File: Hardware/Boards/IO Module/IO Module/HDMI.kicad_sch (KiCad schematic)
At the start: 57 parts, among them J4 HDMI_A, U19 TPS74801AWDRC, U20 SN75DP159RGZ, U21 TXB0108DQSR, U22 TXB0101DCK

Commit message: Completed IO Module PCB Layout
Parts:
- R80: value 10K -> 100K
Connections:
- net +3V3: now also R80.2
- net GND: no longer R80.1
- net HDMI_F_I2C_EN: now also U21.1 (A1); no longer U21.2 (A2)
- net HDMI_F_SWAP: now also U21.2 (A2); no longer U21.1 (A1)
- net HDMI_I2C_EN: now also U21.20 (B1); no longer U21.19 (B2)
- net HDMI_SWAP: now also U21.19 (B2); no longer U21.20 (B1)
- net at U21.6 (OE): now also R80.1; no longer R80.2
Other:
- moved on the sheet: R80
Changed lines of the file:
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@@
 	(wire
 		(pts
-			(xy 275.59 123.19) (xy 273.05 123.19)
-		)
-		(stroke
-			(width 0)
-			(type default)
-		)
-	)
-	(wire
-		(pts
 			(xy 340.36 101.6) (xy 340.36 102.87)
 		)
@@
 	(wire
 		(pts
-			(xy 273.05 156.21) (xy 273.05 157.48)
-		)
-		(stroke
-			(width 0)
-			(type default)
-		)
-	)
-	(wire
-		(pts
 			(xy 106.68 213.36) (xy 106.68 194.31)
 		)
@@
 	(wire
 		(pts
+			(xy 266.7 123.19) (xy 266.7 121.92)
+		)
+		(stroke
+			(width 0)
+			(type default)
+		)
+	)
+	(wire
+		(pts
 			(xy 31.75 54.61) (xy 31.75 55.88)
 		)
@@
 	(wire
 		(pts
-			(xy 273.05 123.19) (xy 273.05 148.59)
-		)
-		(stroke
-			(width 0)
-			(type default)
-		)
-	)
-	(wire
-		(pts
 			(xy 97.79 196.85) (xy 100.33 196.85)
 		)
@@
 	(wire
 		(pts
+			(xy 266.7 123.19) (xy 275.59 123.19)
+		)
+		(stroke
+			(width 0)
+			(type default)
+		)
+	)
+	(wire
+		(pts
 			(xy 321.31 110.49) (xy 321.31 111.76)
 		)
@@
 	(wire
 		(pts
+			(xy 266.7 113.03) (xy 266.7 114.3)
+		)
+		(stroke
+			(width 0)
+			(type default)
+		)
+	)
+	(wire
+		(pts
 			(xy 167.64 120.65) (xy 191.77 120.65)
 		)
@@
 		)
 	)
-	(label "HDMI_F_SWAP"
-		(at 232.41 125.73 0)
-		(fields_autoplaced yes)
-		(effects
-			(font
-				(size 1.27 1.27)
-			)
-			(justify left bottom)
-		)
-	)
 	(label "HDMI_TX_TERM_CTL"
 		(at 321.31 138.43 180)
@@
 		)
 	)
+	(label "HDMI_F_SWAP"
+		(at 232.41 128.27 0)
+		(fields_autoplaced yes)
+		(effects
+			(font
+				(size 1.27 1.27)
+			)
+			(justify left bottom)
+		)
+	)
 	(label "HDMI_AUX_N"
 		(at 138.43 156.21 0)
@@
 		)
 	)
+	(label "HDMI_F_I2C_EN"
+		(at 232.41 125.73 0)
+		(fields_autoplaced yes)
+		(effects
+			(font
+				(size 1.27 1.27)
+			)
+			(justify left bottom)
+		)
+	)
 	(label "HDMI_D0_N"
 		(at 138.43 128.27 0)
@@
 		)
 	)
+	(label "HDMI_SWAP"
+		(at 321.31 128.27 180)
+		(fields_autoplaced yes)
+		(effects
+			(font
+				(size 1.27 1.27)
+			)
+			(justify right bottom)
+		)
+	)
 	(label "PP1V1H_FB"
 		(at 55.88 43.18 0)
@@
 		)
 	)
-	(label "HDMI_F_I2C_EN"
-		(at 232.41 128.27 0)
-		(fields_autoplaced yes)
-		(effects
-			(font
-				(size 1.27 1.27)
-			)
-			(justify left bottom)
-		)
-	)
-	(label "HDMI_SWAP"
-		(at 321.31 125.73 180)
-		(fields_autoplaced yes)
-		(effects
-			(font
-				(size 1.27 1.27)
-			)
-			(justify right bottom)
-		)
-	)
 	(label "HDMI_CON_CLK_P"
 		(at 259.08 68.58 0)
@@
 		)
 	)
+	(label "HDMI_I2C_EN"
+		(at 321.31 125.73 180)
+		(fields_autoplaced yes)
+		(effects
+			(font
+				(size 1.27 1.27)
+			)
+			(justify right bottom)
+		)
+	)
 	(label "HDMI_CEC"
 		(at 138.43 245.11 0)
@@
 		)
 	)
-	(label "HDMI_I2C_EN"
-		(at 321.31 128.27 180)
-		(fields_autoplaced yes)
-		(effects
-			(font
-				(size 1.27 1.27)
-			)
-			(justify right bottom)
-		)
-	)
 	(label "HDMI_F_EQ_SEL"
 		(at 232.41 133.35 0)
@@
 		)
 	)
-	(hierarchical_label "HDMI_SWAP"
-		(shape input)
-		(at 321.31 125.73 0)
-		(fields_autoplaced yes)
-		(effects
-			(font
-				(size 1.27 1.27)
-			)
-			(justify left)
-		)
-	)
 	(hierarchical_label "HDMI_CLK_P"
 		(shape input)
@@
 		)
 	)
-	(hierarchical_label "HDMI_I2C_EN"
-		(shape input)
-		(at 321.31 128.27 0)
-		(fields_autoplaced yes)
-		(effects
-			(font
-				(size 1.27 1.27)
-			)
-			(justify left)
-		)
-	)
 	(hierarchical_label "HDMI_D2_N"
 		(shape input)
@@
 		)
 	)
+	(hierarchical_label "HDMI_SWAP"
+		(shape input)
+		(at 321.31 128.27 0)
+		(fields_autoplaced yes)
+		(effects
+			(font
+				(size 1.27 1.27)
+			)
+			(justify left)
+		)
+	)
 	(hierarchical_label "FPGA_I2C_SDA"
 		(shape input)
@@
 		)
 	)
+	(hierarchical_label "HDMI_I2C_EN"
+		(shape input)
+		(at 321.31 125.73 0)
+		(fields_autoplaced yes)
+		(effects
+			(font
+				(size 1.27 1.27)
+			)
+			(justify left)
+		)
+	)
 	(hierarchical_label "FPGA_I2C_SCL"
 		(shape input)
@@
 	)
 	(symbol
-		(lib_id "power:GND")
-		(at 273.05 157.48 0)
-		(unit 1)
-		(exclude_from_sim no)
-		(in_bom yes)
-		(on_board yes)
-		(dnp no)
-		(property "Reference" "#PWR0245"
-			(at 273.05 161.29 0)
-			(effects
-				(font
-					(size 1.27 1.27)
-				)
-				(hide yes)
-			)
-		)
-		(property "Value" "GND"
-			(at 273.05 161.29 0)
-			(effects
-				(font
-					(size 1.27 1.27)
-				)
-			)
-		)
-		(property "Footprint" ""
-			(at 273.05 157.48 0)
-			(effects
-				(font
-					(size 1.27 1.27)
-				)
-				(hide yes)
-			)
-		)
-		(property "Datasheet" ""
-			(at 273.05 157.48 0)
-			(effects
-				(font
-					(size 1.27 1.27)
-				)
-				(hide yes)
-			)
-		)
-		(property "Description" "Power symbol creates a global label with name \"GND\" , ground"
-			(at 273.05 157.48 0)
-			(effects
-				(font
-					(size 1.27 1.27)
-				)
-				(hide yes)
-			)
-		)
-		(pin "1"
-		)
-		(instances
-			(project "IO Module"
-				(path "/884396b6-238b-495e-b731-e47ad2523f76/dcc99803-8acd-4632-9c0b-7f677477cf65/84e0983c-4a92-4326-b25d-d105fd964129"
-					(reference "#PWR0245")
-					(unit 1)
-				)
-			)
-		)
-	)
-	(symbol
 		(lib_id "power:+1V8")
 		(at 204.47 222.25 0)
@@
 	(symbol
 		(lib_id "Device:R_US")
-		(at 273.05 152.4 180)
+		(at 266.7 118.11 180)
 		(unit 1)
 		(exclude_from_sim no)
@@
 		(dnp no)
 		(property "Reference" "R80"
-			(at 277.495 153.67 0)
+			(at 271.145 119.38 0)
 			(effects
 				(font
@@
 			)
 		)
-		(property "Value" "10K"
-			(at 277.495 151.13 0)
+		(property "Value" "100K"
+			(at 271.145 116.84 0)
 			(effects
 				(font
@@
 		)
 		(property "Footprint" "Resistor_SMD:R_0201_0603Metric"
-			(at 272.034 152.146 90)
+			(at 265.684 117.856 90)
 			(effects
 				(font
@@
 		)
 		(property "Datasheet" "~"
-			(at 273.05 152.4 0)
+			(at 266.7 118.11 0)
 			(effects
 				(font
@@
 		)
 		(property "Description" "Resistor, US symbol"
-			(at 273.05 152.4 0)
+			(at 266.7 118.11 0)
 			(effects
 				(font
@@
 					(unit 1)
 				)
+			)
+		)
+	)
+	(symbol
+		(lib_id "power:+3V3")
+		(at 266.7 113.03 0)
+		(unit 1)
+		(exclude_from_sim no)
+		(in_bom yes)
+		(on_board yes)
+		(dnp no)
+		(property "Reference" "#PWR0159"
+			(at 266.7 116.84 0)
+			(effects
+				(font
+					(size 1.27 1.27)
+				)
+				(hide yes)
+			)
+		)
+		(property "Value" "+3V3"
+			(at 266.7 109.22 0)
+			(effects
+				(font
+					(size 1.27 1.27)
+				)
+			)
+		)
+		(property "Footprint" ""
+			(at 266.7 113.03 0)
+			(effects
+				(font
+					(size 1.27 1.27)
+				)
+				(hide yes)
+			)
+		)
+		(property "Datasheet" ""
+			(at 266.7 113.03 0)
+			(effects
+				(font
+					(size 1.27 1.27)
+				)
+				(hide yes)
+			)
+		)
+		(property "Description" "Power symbol creates a global label with name \"+3V3\""
+			(at 266.7 113.03 0)
+			(effects
+				(font
+					(size 1.27 1.27)
+				)
+				(hide yes)
+			)
+		)
+		(pin "1"
+		)
+		(instances
+			(project "IO Module"
+				(path "/884396b6-238b-495e-b731-e47ad2523f76/dcc99803-8acd-4632-9c0b-7f677477cf65/84e0983c-4a92-4326-b25d-d105fd964129"
+					(reference "#PWR0159")
+					(unit 1)
+				)

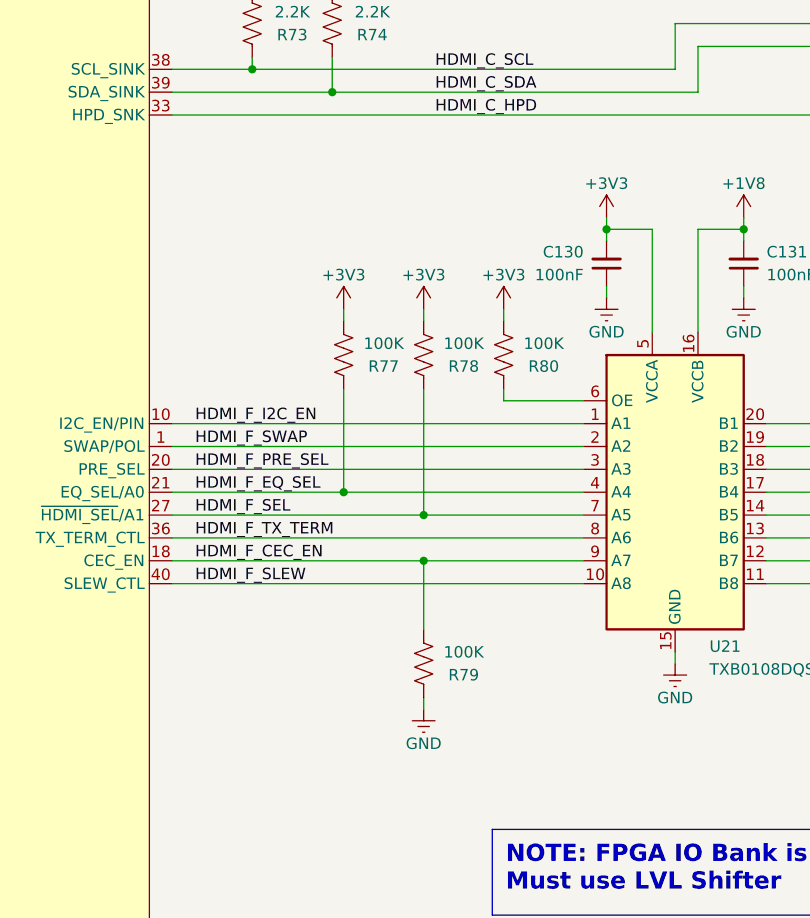
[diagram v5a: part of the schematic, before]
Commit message: Cleaned up routing for IO module
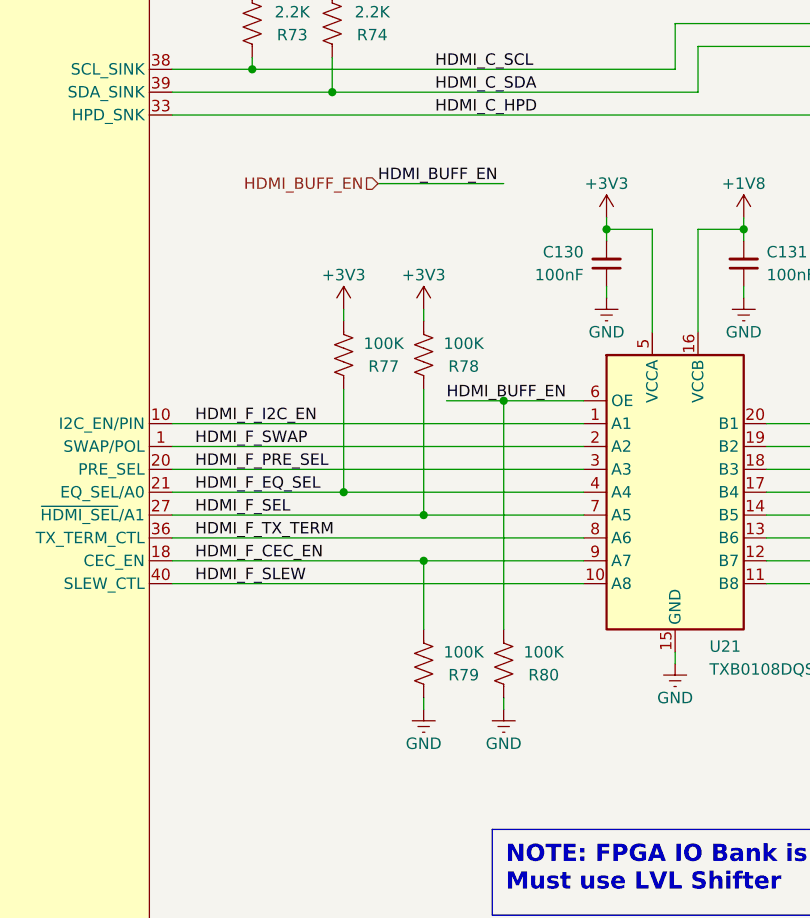
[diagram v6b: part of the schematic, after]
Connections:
- net +3V3: no longer R80.2
- net GND: now also R80.1
- net HDMI_BUFF_EN: now reaches U21.6 (OE)
- net HDMI_BUFF_EN: now also R80.2; no longer R80.1
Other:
- moved on the sheet: R80
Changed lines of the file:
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@@
 	)
 	(junction
+		(at 266.7 123.19)
+		(diameter 0)
+		(color 0 0 0 0)
+	)
+	(junction
 		(at 168.91 78.74)
 		(diameter 0)
@@
 	(wire
 		(pts
+			(xy 266.7 123.19) (xy 266.7 148.59)
+		)
+		(stroke
+			(width 0)
+			(type default)
+		)
+	)
+	(wire
+		(pts
 			(xy 154.94 184.15) (xy 191.77 184.15)
 		)
@@
 	(wire
 		(pts
-			(xy 266.7 123.19) (xy 266.7 121.92)
+			(xy 266.7 123.19) (xy 275.59 123.19)
 		)
 		(stroke
@@
 	(wire
 		(pts
+			(xy 266.7 156.21) (xy 266.7 157.48)
+		)
+		(stroke
+			(width 0)
+			(type default)
+		)
+	)
+	(wire
+		(pts
 			(xy 167.64 142.24) (xy 191.77 142.24)
 		)
@@
 	(wire
 		(pts
+			(xy 252.73 99.06) (xy 266.7 99.06)
+		)
+		(stroke
+			(width 0)
+			(type default)
+		)
+	)
+	(wire
+		(pts
 			(xy 190.5 55.88) (xy 191.77 55.88)
 		)
@@
 	(wire
 		(pts
-			(xy 266.7 123.19) (xy 275.59 123.19)
+			(xy 260.35 123.19) (xy 266.7 123.19)
 		)
 		(stroke
@@
 	(wire
 		(pts
-			(xy 266.7 113.03) (xy 266.7 114.3)
-		)
-		(stroke
-			(width 0)
-			(type default)
-		)
-	)
-	(wire
-		(pts
 			(xy 167.64 120.65) (xy 191.77 120.65)
 		)
@@
 		)
 	)
+	(label "HDMI_BUFF_EN"
+		(at 260.35 123.19 0)
+		(fields_autoplaced yes)
+		(effects
+			(font
+				(size 1.27 1.27)
+			)
+			(justify left bottom)
+		)
+	)
 	(label "HDMI_TX_TERM_CTL"
 		(at 321.31 138.43 180)
@@
 		)
 	)
+	(label "HDMI_BUFF_EN"
+		(at 252.73 99.06 0)
+		(fields_autoplaced yes)
+		(effects
+			(font
+				(size 1.27 1.27)
+			)
+			(justify left bottom)
+		)
+	)
 	(label "HDMI_CLK_N"
 		(at 138.43 142.24 0)
@@
 		)
 	)
+	(hierarchical_label "HDMI_BUFF_EN"
+		(shape input)
+		(at 252.73 99.06 180)
+		(fields_autoplaced yes)
+		(effects
+			(font
+				(size 1.27 1.27)
+			)
+			(justify right)
+		)
+	)
 	(hierarchical_label "HDMI_D2_N"
 		(shape input)
@@
 	(symbol
 		(lib_id "power:GND")
+		(at 266.7 157.48 0)
+		(unit 1)
+		(exclude_from_sim no)
+		(in_bom yes)
+		(on_board yes)
+		(dnp no)
+		(property "Reference" "#PWR088"
+			(at 266.7 161.29 0)
+			(effects
+				(font
+					(size 1.27 1.27)
+				)
+				(hide yes)
+			)
+		)
+		(property "Value" "GND"
+			(at 266.7 161.29 0)
+			(effects
+				(font
+					(size 1.27 1.27)
+				)
+			)
+		)
+		(property "Footprint" ""
+			(at 266.7 157.48 0)
+			(effects
+				(font
+					(size 1.27 1.27)
+				)
+				(hide yes)
+			)
+		)
+		(property "Datasheet" ""
+			(at 266.7 157.48 0)
+			(effects
+				(font
+					(size 1.27 1.27)
+				)
+				(hide yes)
+			)
+		)
+		(property "Description" "Power symbol creates a global label with name \"GND\" , ground"
+			(at 266.7 157.48 0)
+			(effects
+				(font
+					(size 1.27 1.27)
+				)
+				(hide yes)
+			)
+		)
+		(pin "1"
+		)
+		(instances
+			(project "IO Module"
+				(path "/884396b6-238b-495e-b731-e47ad2523f76/dcc99803-8acd-4632-9c0b-7f677477cf65/84e0983c-4a92-4326-b25d-d105fd964129"
+					(reference "#PWR088")
+					(unit 1)
+				)
+			)
+		)
+	)
+	(symbol
+		(lib_id "power:GND")
 		(at 167.64 60.96 0)
 		(unit 1)
@@
 	(symbol
 		(lib_id "Device:R_US")
-		(at 266.7 118.11 180)
+		(at 266.7 152.4 180)
 		(unit 1)
 		(exclude_from_sim no)
@@
 		(dnp no)
 		(property "Reference" "R80"
-			(at 271.145 119.38 0)
+			(at 271.145 153.67 0)
 			(effects
 				(font
@@
 		)
 		(property "Value" "100K"
-			(at 271.145 116.84 0)
+			(at 271.145 151.13 0)
 			(effects
 				(font
@@
 		)
 		(property "Footprint" "Resistor_SMD:R_0201_0603Metric"
-			(at 265.684 117.856 90)
+			(at 265.684 152.146 90)
 			(effects
 				(font
@@
 		)
 		(property "Datasheet" "~"
-			(at 266.7 118.11 0)
+			(at 266.7 152.4 0)
 			(effects
 				(font
@@
 		)
 		(property "Description" "Resistor, US symbol"
-			(at 266.7 118.11 0)
+			(at 266.7 152.4 0)
 			(effects
 				(font
@@
 					(unit 1)
 				)
-			)
-		)
-	)
-	(symbol
-		(lib_id "power:+3V3")
-		(at 266.7 113.03 0)
-		(unit 1)
-		(exclude_from_sim no)
-		(in_bom yes)
-		(on_board yes)
-		(dnp no)
-		(property "Reference" "#PWR0159"
-			(at 266.7 116.84 0)
-			(effects
-				(font
-					(size 1.27 1.27)
-				)
-				(hide yes)
-			)
-		)
-		(property "Value" "+3V3"
-			(at 266.7 109.22 0)
-			(effects
-				(font
-					(size 1.27 1.27)
-				)
-			)
-		)
-		(property "Footprint" ""
-			(at 266.7 113.03 0)
-			(effects
-				(font
-					(size 1.27 1.27)
-				)
-				(hide yes)
-			)
-		)
-		(property "Datasheet" ""
-			(at 266.7 113.03 0)
-			(effects
-				(font
-					(size 1.27 1.27)
-				)
-				(hide yes)
-			)
-		)
-		(property "Description" "Power symbol creates a global label with name \"+3V3\""
-			(at 266.7 113.03 0)
-			(effects
-				(font
-					(size 1.27 1.27)
-				)
-				(hide yes)
-			)
-		)
-		(pin "1"
-		)
-		(instances
-			(project "IO Module"
-				(path "/884396b6-238b-495e-b731-e47ad2523f76/dcc99803-8acd-4632-9c0b-7f677477cf65/84e0983c-4a92-4326-b25d-d105fd964129"
-					(reference "#PWR0159")
-					(unit 1)
-				)

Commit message: Using new DP to HDMI IC
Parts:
- removed C139, C141, C142: 100nF, Capacitor_SMD:C_0201_0603Metric, symbol Device:C_Small
- removed D8: BAS516, Diode_SMD:D_SOD-523, symbol Diode:BAS516
- removed R82: 1K, Resistor_SMD:R_0201_0603Metric, symbol Device:R_US
- removed R88: 27K, Resistor_SMD:R_0201_0603Metric, symbol Device:R_US
- removed U20: SN75DP159RGZ, Package_DFN_QFN:QFN-48-1EP_7x7mm_P0.5mm_EP5.1x5.1mm, symbol IO_Module:SN75DP159
- removed U22: TXB0101DCK, Package_TO_SOT_SMD:SOT-363_SC-70-6, symbol Logic_LevelTranslator:TXB0101DCK
- added C153: 1uF, Capacitor_SMD:C_0201_0603Metric, symbol Device:C_Small
- added C154, C155, C156, C43: 100nF, Capacitor_SMD:C_0201_0603Metric, symbol Device:C_Small
- added R34: 33R, Resistor_SMD:R_0201_0603Metric, symbol Device:R_US
- added R35: 1K, Resistor_SMD:R_0201_0603Metric, symbol Device:R_US
- added U10, U25: TPD4E02B04DQA, Package_SON:USON-10_2.5x1.0mm_P0.5mm, symbol Power_Protection:TPD4E02B04DQA
- added U20: PCA9517ATP, IO_Module:HWSON8_SOT1069-2_NXP, symbol IO_Module:PCA9517A
- added U27: L78L05_SOT89, Package_TO_SOT_SMD:SOT-89-3, symbol Regulator_Linear:L78L05_SOT89
- added U5: SN75DP159RSB, Package_DFN_QFN:QFN-40-1EP_5x5mm_P0.4mm_EP3.6x3.6mm, symbol IO_Module:SN75DP159RSB
- added U7: TPD5S116, IO_Module:15DSBGA-TEXAS, symbol IO_Module:TPS5S116
- C113: value 1uF -> 100nF
- R75: value 0R -> 1K
- R79: value 100K -> 1K
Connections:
- net HDMI_AUX_N is gone; now on net +3V3: C138.2
- net HDMI_CEC_EN is gone; now on net HDMI_I2C_EN: U21.12 (B7)
- net HDMI_C_AUX_N is gone; now on net GND: C138.1
- net HDMI_F_TX_TERM is gone; now on net HDMI_F_EQ_SEL: U21.8 (A6)
- net HDMI_SWAP is gone; now on net HDMI_OE: U21.19 (B2)
- net HDMI_TX_TERM_CTL is gone; now on net HDMI_EQ_SEL: U21.13 (B6)
- net +1V8: now also C113.2, R75.2, C154.2, R35.2, U20.7 (VCC_A), U7.A2 (VCCA); no longer R81.2
- net +3V3: now also R79.2, R81.2, U20.6 (VCC_B), U5.11 (VCC), U5.37 (VCC)
- net GND: now also C113.1, C153.2, C154.1, C155.1, C156.1, C43.1, U10.3 (G), U10.8 (G), U20.2 (GND), U20.9 (EPAD), U25.3 (G), U25.8 (G), U27.2 (GND), U5.15 (GND), U5.35 (GND), U5.41 (EPAD), U7.B2 (GND), U7.D2 (GND); no longer C113.2, R75.1, R79.1
- net HDMI_CEC: now also U7.A1 (CEC_SYS)
- net HDMI_CON_CLK_N: now also U25.5 (IO4), U25.6 (NC), U5.21 (OUT_CLKn)
- net HDMI_CON_CLK_P: now also U25.4 (IO3), U25.7 (NC), U5.22 (OUT_CLKp)
- net HDMI_CON_D0_N: now also U25.2 (IO2), U25.9 (NC), U5.24 (OUT_D0n)
- net HDMI_CON_D0_P: now also U25.1 (IO1), U25.10 (NC), U5.25 (OUT_D0p)
- net HDMI_CON_D1_N: now also U10.5 (IO4), U10.6 (NC), U5.26 (OUT_D1n)
- net HDMI_CON_D1_P: now also U10.4 (IO3), U10.7 (NC), U5.27 (OUT_D1p)
- net HDMI_CON_D2_N: now also U10.2 (IO2), U10.9 (NC), U5.29 (OUT_D2n)
- net HDMI_CON_D2_P: now also U10.1 (IO1), U10.10 (NC), U5.30 (OUT_D2p)
- net HDMI_C_CEC: now also U7.A3 (CEC_CON)
- net HDMI_C_CLK_N: now also U5.10 (IN_CLKn)
- net HDMI_C_CLK_P: now also U5.9 (IN_CLKp)
- net HDMI_C_D0_N: now also U5.7 (IN_D0n)
- net HDMI_C_D0_P: now also U5.6 (IN_D0p)
- net HDMI_C_D1_N: now also U5.5 (IN_D1n)
- net HDMI_C_D1_P: now also U5.4 (IN_D1p)
- net HDMI_C_D2_N: now also U5.2 (IN_D2n)
- net HDMI_C_D2_P: now also U5.1 (IN_D2p)
- net HDMI_C_HPD: now also U5.28 (HPD_SNK), U7.E3 (HPD_CON)
- net HDMI_C_SCL: now also U5.32 (SCL_SINK), U7.B3 (SCL_CON)
- net HDMI_C_SDA: now also U5.33 (SDA_SINK), U7.C3 (SDA_CON)
- net HDMI_EQ_SEL: no longer U21.17 (B4)
- net HDMI_F_EQ_SEL: now also U5.17 (EQ_SEL/A0); no longer U21.4 (A4)
- net HDMI_F_I2C_EN: now also U21.9 (A7), U5.8 (I2C_EN/PIN); no longer U21.1 (A1)
- net HDMI_F_PRE_SEL: now also U21.7 (A5), U5.16 (PRE_SEL); no longer U21.3 (A3)
- net HDMI_F_SEL: now also U21.3 (A3), U5.23 (~{HDMI_SEL}/A1); no longer U21.7 (A5)
- net HDMI_F_SLEW: now also U21.1 (A1), U5.34 (SLEW_CTL); no longer U21.10 (A8)
- net HDMI_HPD_SRC: now also U21.17 (B4), U7.E1 (HPD_SYS)
- net HDMI_I2C_EN: no longer U21.20 (B1)
- net HDMI_OE: no longer C140.2
- net HDMI_PRE_SEL: now also U21.14 (B5); no longer U21.18 (B3)
- net HDMI_SCL_CTL: now also U5.13 (SCL_CTL)
- net HDMI_SCL_SRC: now also R35.1, U20.1 (SDA_A); no longer R81.1
- net HDMI_SDA_CTL: now also U5.14 (SDA_CTL)
- net HDMI_SDA_SRC: now also R75.1, U20.8 (SCL_A)
- net HDMI_SEL: now also U21.18 (B3); no longer U21.14 (B5)
- net HDMI_SLEW_CTL: now also U21.20 (B1); no longer U21.11 (B8)
- net PP_1V1_HDMI: now also U5.12 (VDD), U5.19 (VDD), U5.20 (VDD), U5.31 (VDD), U5.40 (VDD)
- net at R87.2: now also U5.18 (Vsadj)
- net UTIL_CON: now reaches J4.14 (UTILITY)
- net UTIL_CON: now also U7.E2 (UTI_CON); no longer R75.2
- net +5V renamed 5V_CON
- net 5V_CON: now also C156.2, U7.D3 (5V_CON); no longer C113.1
- removed net HDMI_F_CEC_EN: R79.2, U21.9 (A7)
- net HDMI_F_SWAP renamed HDMI_F_OE
- net HDMI_F_OE: now also C140.2, U5.36 (OE)
- new net: R34.1, U5.3 (HPD_SRC)
- new net 5V_SYS: C155.2, C43.2, U27.1 (OUT), U7.D1 (5V_SYS)
- new net HDMI_F_HPD_SRC: R34.2, U21.4 (A4)
- new net HDMI_SDA_SRC_EN: U20.3 (EN)
- new net PP_VUSB_R: C153.1, U27.3 (IN)
- new net SCL_SRC: R81.1, U20.5 (SCL_B), U5.38 (SCL_SRC)
- new net SDA_SRC: R79.1, U20.4 (SDA_B), U5.39 (SDA_SRC)
- new net TPD5_EN: U7.C2 (EN)
- no-connect marks 0 -> 4
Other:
- note added: "HDMI ESD"
- moved on the sheet: C118, C119, C120, C121, C122, C123, C124, C125, C126, C127, C128, C129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
